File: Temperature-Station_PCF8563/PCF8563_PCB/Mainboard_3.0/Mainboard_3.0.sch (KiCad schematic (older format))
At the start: 47 parts, among them J1 Breakout_Left, J10 I2C Breakout, J2 Socket_Left, J3 Jack-DC, J4 Breakout_Right, J5 Socket_Right, J6 1-Wire, J7 sensor_internal, J8 Prog, J9 SD_Card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

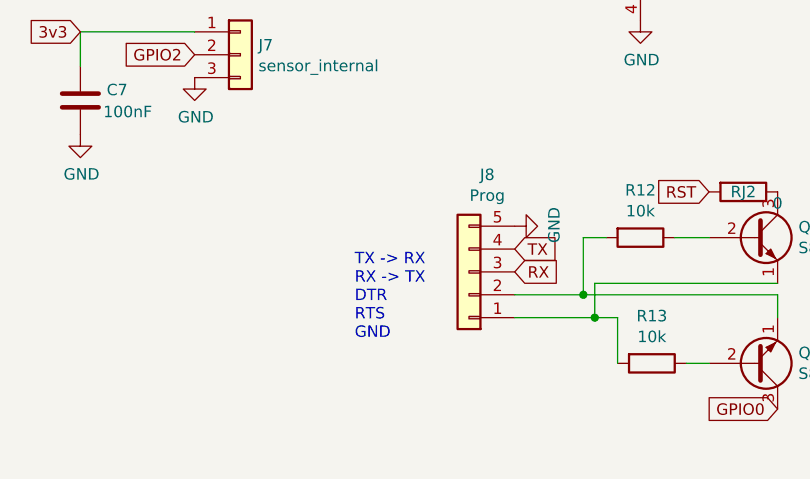
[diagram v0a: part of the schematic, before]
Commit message: Large update
Muxtemp:
Optimized timing
Added library.properies
No compiler warnings

Czas:
No compiler warnings

I2C Expander:
Minor optimization
Added 1wire bypass (will require jumpers)
Added debug mode
No idea why but DHT22 is detected as DHT21
Improved stability

PCF8563 version:
Defaults are in sketch, not settingsHandler library
Fixed sensor view (renaming, deleting etc)
Removed 1wire circuit (one spare GPIO port)
Completely migrated to use Muxtemp without bypassing 1wire
Added Muxtemp summary on boot
Slight formatting on boot summary
Automatic sensor refreshing in JSON file
Fixed softAP mode for config
updateNTP now returns false if cannot resolve hostname
Begin to fix configuration page
Added authentication when connecting to any site

settingsHandler:
removed defaults, if you want something do it outside
no sensitive data is returned
Added NTP options
Added configurable path for updateServer
Added webAuthenticate (uses authenticate() from ESP8266WebServer)
toDo: change some voids to booleans to check if field was updated correctly

Mainboard 3.0:
Changed order in description of programming/UART header to match pins
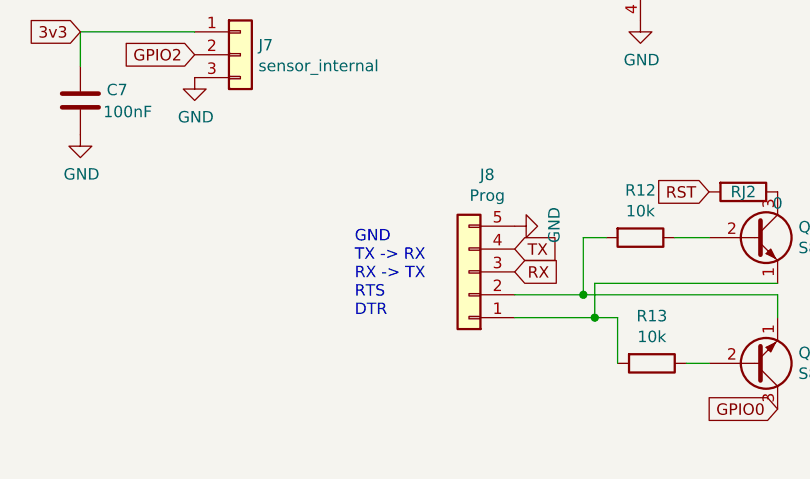
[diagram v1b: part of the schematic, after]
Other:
- note added: "GND\nTX -> RX\nRX -> TX\nRTS\nDTR"
- note removed: "TX -> RX\nRX -> TX\nDTR\nRTS\nGND"
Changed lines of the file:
@@
 	-1   0    0    1
 $EndComp
-Text Notes 7950 5700 0    50   ~ 0
-TX -> RX\nRX -> TX\nDTR\nRTS\nGND
+Text Notes 7950 5600 0    50   ~ 0
+GND\nTX -> RX\nRX -> TX\nRTS\nDTR
 Text GLabel 3350 3350 0    50   Input ~ 0
 RX
